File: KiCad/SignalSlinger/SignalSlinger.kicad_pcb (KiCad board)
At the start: 4 copper layers, 94.1 x 59.1 mm, 124 parts, among them J101 Conn_01x02, J102 Conn_01x03, J103 Conn_01x02, J104 Conn_01x02, J105 Conn_01x04, J106 Conn_01x02, J107 DB9 Female, J201 Barrel_Jack_Switch, J203 External Fan Power, J204 Controlled Power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

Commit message: Button Tweak
o Updated on-PCB pushbutton to be the same one used for SignalSnagger
o Updated location of pushbutton to reach only to the edge of the PCB
o Updated Gerbers
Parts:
- SW101: footprint Button_Switch_SMD:SW_SPST_TL3305A -> Button_Switch_SMD:SW_SPST_TL1014BF160QG
- moved SW101 0.31 mm to (82.2, 116.2)
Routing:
- net Net-(C104-Pad1): track 69.8 -> 69.1 mm

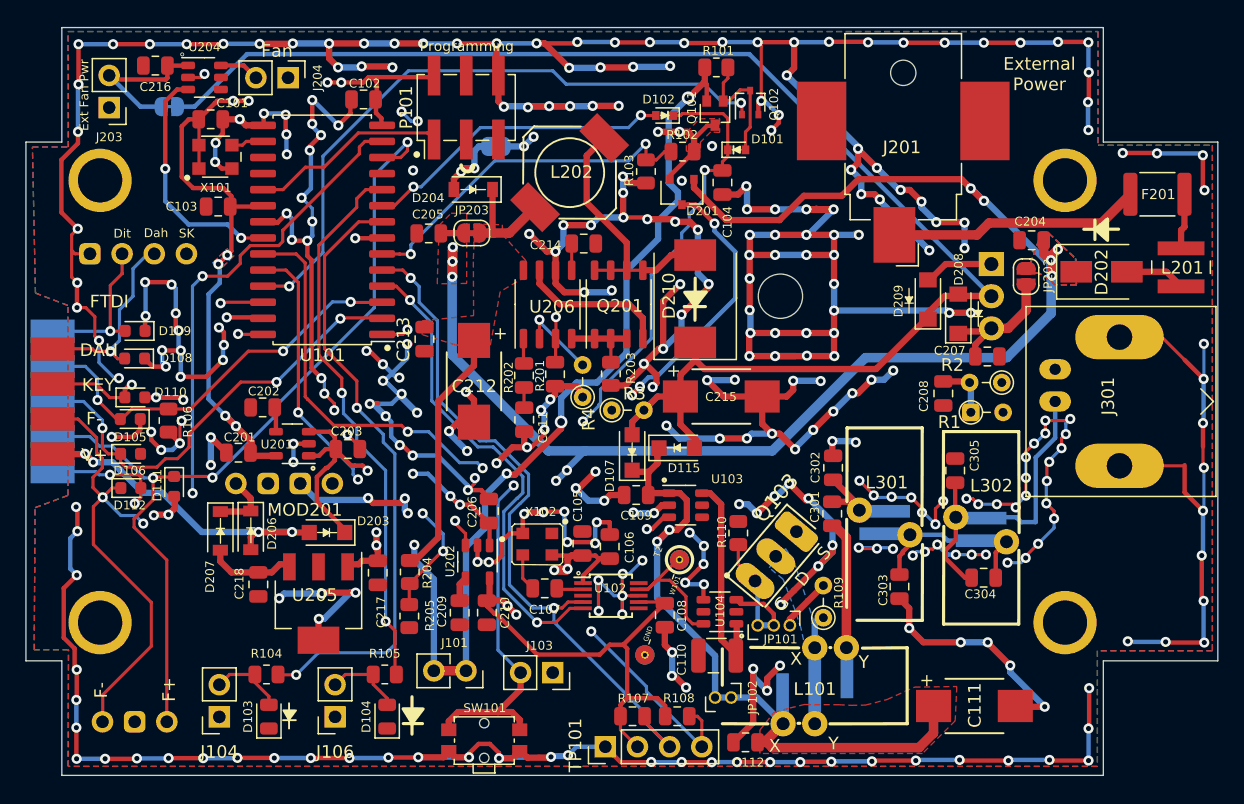
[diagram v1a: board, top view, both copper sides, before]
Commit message: Design Updates
oThe boost regulator was removed from the design.
oAn additional load switch was added to the design.
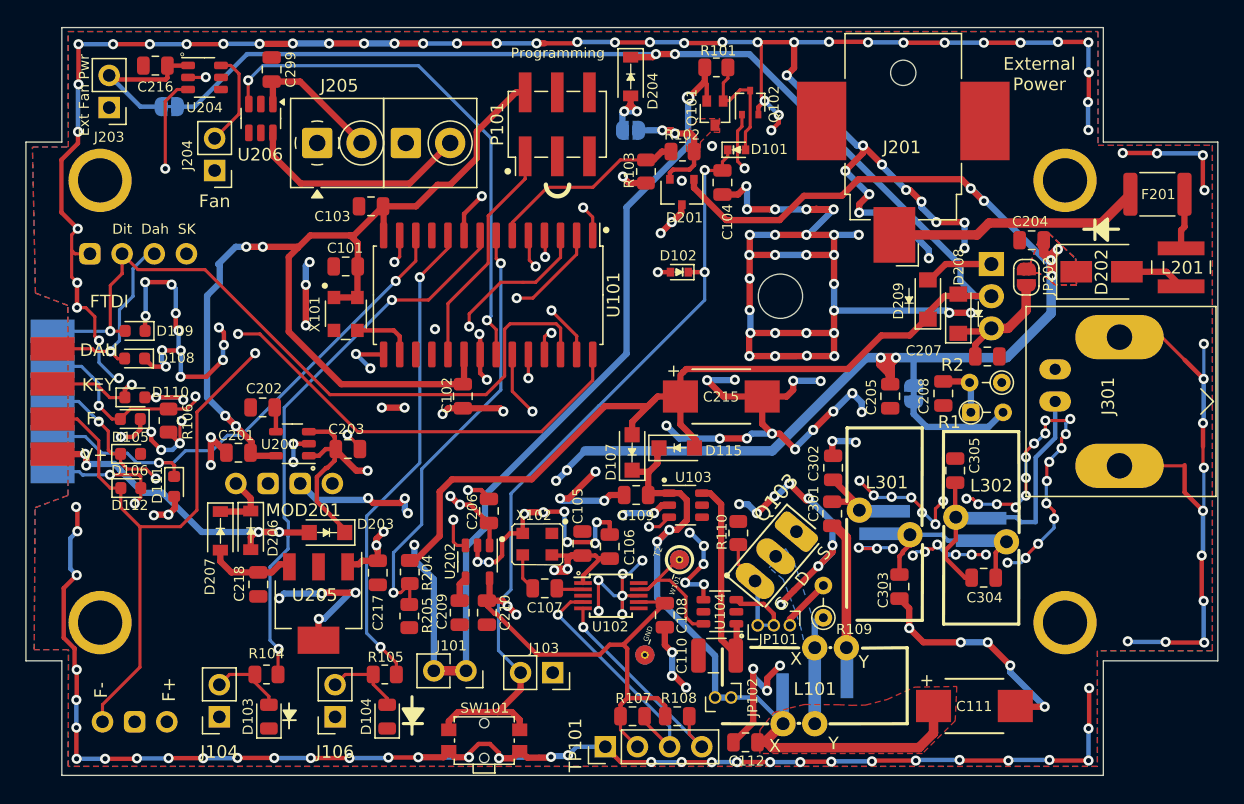
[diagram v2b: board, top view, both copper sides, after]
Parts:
- removed C211: 10nF, Capacitor_SMD:C_0805_2012Metric
- removed C212: 47uF low ESR, Capacitors:C_2917
- removed C213: 10uF, Capacitor_SMD:C_0805_2012Metric
- removed C214: 1uF, Capacitor_SMD:C_0805_2012Metric
- removed D210: B530, Diode_SMD:D_SMC
- removed L202: 6.8uH, Inductors:CDR7D28MN
- removed Q201: RJK0354DSP, Package_SO:SOIC-8_3.9x4.9mm_P1.27mm
- removed R201, R202: 10k, Capacitor_SMD:C_0805_2012Metric
- removed R203: 0.01 0.5W, Resistor_SMD:R_0805_2012Metric
- removed R3, R4: TBD, Resistor_THT:R_Axial_DIN0204_L3.6mm_D1.6mm_P2.54mm_Vertical
- added C299: 10uF, Capacitor_SMD:C_0805_2012Metric, F.Cu at (65.4, 63.2)
- added J205: Controlled Bat Pwr, TerminalBlock_4Ucon:TerminalBlock_4Ucon_1x02_P3.50mm_Horizontal, F.Cu at (69.0, 69.0)
- C111, C215: footprint Capacitors:C_2917 -> Capacitor_Tantalum_SMD:C_2917
- J204: value Controlled Power -> Controlled Fan Power
- JP203: moved to B.Cu
- U206: value MIC2196YM -> TPS22810DBVT; footprint Package_SO:SOIC-8_3.9x4.9mm_P1.27mm -> Package_TO_SOT_SMD:SOT-23-6
- moved C205 38.6 mm to (114.2, 89.0), turned to 90 degrees
- moved JP203 37.1 mm to (116.1, 88.8), turned to -90 degrees
- moved U206 27.0 mm to (64.5, 67.1), turned to -90 degrees
- moved C102 24.7 mm to (80.5, 89.0), turned to -90 degrees
- moved X101 16.1 mm to (71.2, 82.5), turned to 0 degrees
- moved C101 15.8 mm to (71.2, 78.8), turned to 180 degrees
- moved D204 15.3 mm to (93.8, 63.8), turned to -90 degrees
- moved U101 14.1 mm to (82.5, 81.0), turned to -90 degrees
- moved D102 12.4 mm to (97.6, 79.2)
- moved C103 12.1 mm to (73.2, 74.0)
- moved JP204 10.7 mm to (93.8, 68.0)
- moved J204 9.34 mm to (60.9, 71.2), turned to 180 degrees
- moved P101 7.31 mm to (88.0, 67.5)
- moved JP202 0.05 mm to (125.0, 79.6)
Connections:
- net Power_enable renamed Master_Power_enable
- D204 pad 1: Net-(C212-Pad1) -> Vdrive
- JP203 pad 2: Net-(C212-Pad1) -> Vdrive
- R204 pad 2: Net-(C212-Pad1) -> Vdrive
- REF** pad : (no net) -> GND (x4)
- U101 pad 1: BOOST_PWR_ENABLE -> Fan_Contr
- U101 pad 22: Fan_Contr -> Ext_Bat_Contr
- U206 pad 2: Net-(R3-Pad1) -> GND
- U206 pad 3: BOOST_PWR_ENABLE -> Ext_Bat_Contr
- U206 pad 4: Net-(Q201-Pad1) -> unconnected-(U206-CT-Pad4)
- U206 pad 5: Net-(C214-Pad1) -> unconnected-(U206-QOD-Pad5)
- U206 pad 6: GND -> Net-(J205-Pin_4)
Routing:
- net GND: track 895.3 -> 745.0 mm, vias 340 -> 278
- net Ext_Bat_Contr: track 0.00 -> 41.4 mm, vias 0 -> 2
- net Vdrive: track 126.3 -> 162.1 mm, vias 0 -> 2
- net Paddle_Dit: track 25.0 -> 57.9 mm, vias 2 -> 1
- net Straightkey: track 29.3 -> 62.1 mm
- net Net-(C212-Pad1): track 28.0 -> 0.00 mm
- net Fan_Contr: track 18.3 -> 45.8 mm
- net Paddle Dah: track 27.8 -> 55.2 mm
- net FET_DRIVER_ENABLE: track 47.6 -> 21.4 mm, vias 3 -> 2
- net Master_Power_enable: track 51.3 -> 27.3 mm
- net Net-(D210-Pad2): track 20.8 -> 0.00 mm
- net V_ext: track 137.8 -> 118.5 mm, vias 12 -> 11
- net Net-(D106-A1): track 35.3 -> 54.0 mm
- net Net-(D105-A2): track 32.1 -> 50.7 mm
- net +VSW: track 28.3 -> 9.99 mm, vias 4 -> 2
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- removed copper zone on B.Cu, net +3V3
- removed copper zone on F.Cu, net +3V3
- removed copper zone on F.Cu, net Net-(C212-Pad1)
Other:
- board text added: "SignalSlinger 80m Radio-O Fox Transmitter Ver: 3.5; Date: 10-Sep-2025"
- board text removed: "SignalSlinger 80m Radio-O Fox Transmitter Ver: 3.4; Date: 14-Jun-2024"

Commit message: Production Hardware Design Updates
Ver 3.5
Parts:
- added REF**: MountingHole_2mm, MountingHole:MountingHole_2mm, F.Cu at (76.1, 62.5)
- added REF**: MountingHole_2mm, MountingHole:MountingHole_2mm, F.Cu at (72.5, 62.5)
- L302: footprint Inductors:Toroid_T-60_2TH_Vertical -> Inductor_THT:Toroid_T-60_2TH_Vertical2
- moved C305 9.16 mm to (126.2, 101.0), turned to 0 degrees
- moved C303 1.84 mm to (115.1, 102.2)
- moved C304 1.69 mm to (121.3, 101.7), turned to 180 degrees
- moved C111 1.49 mm to (122.3, 113.9)
- moved L101 1.27 mm to (109.6, 111.8)
- turned L302 to 0 degrees
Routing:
- net GND: track 745.0 -> 809.5 mm, vias 278 -> 299
- net Ext_Bat_Contr: track 41.4 -> 33.6 mm
- net Net-(J301-In): track 25.6 -> 18.3 mm
- net Vdrive: track 162.1 -> 168.0 mm
- net Net-(C303-Pad2): track 12.6 -> 8.87 mm
- net Paddle Dah: track 55.2 -> 57.4 mm
- net Master_Power_enable: track 27.3 -> 29.3 mm
- net Frequency Up: track 61.8 -> 63.0 mm
- net Paddle_Dit: track 57.9 -> 58.9 mm
- net Net-(JP102-B): track 23.6 -> 24.3 mm
- net Net-(C301-Pad2): track 5.00 -> 4.36 mm
- net Frequency Down: track 65.2 -> 64.7 mm
- net V3V3_PWR_ENABLE: track 18.5 -> 19.1 mm
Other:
- board text added: "+BAT"
- board text added: "External Battery Control"
- board text added: "Key"
- board text added: "VSW"
- board text removed: "SK"

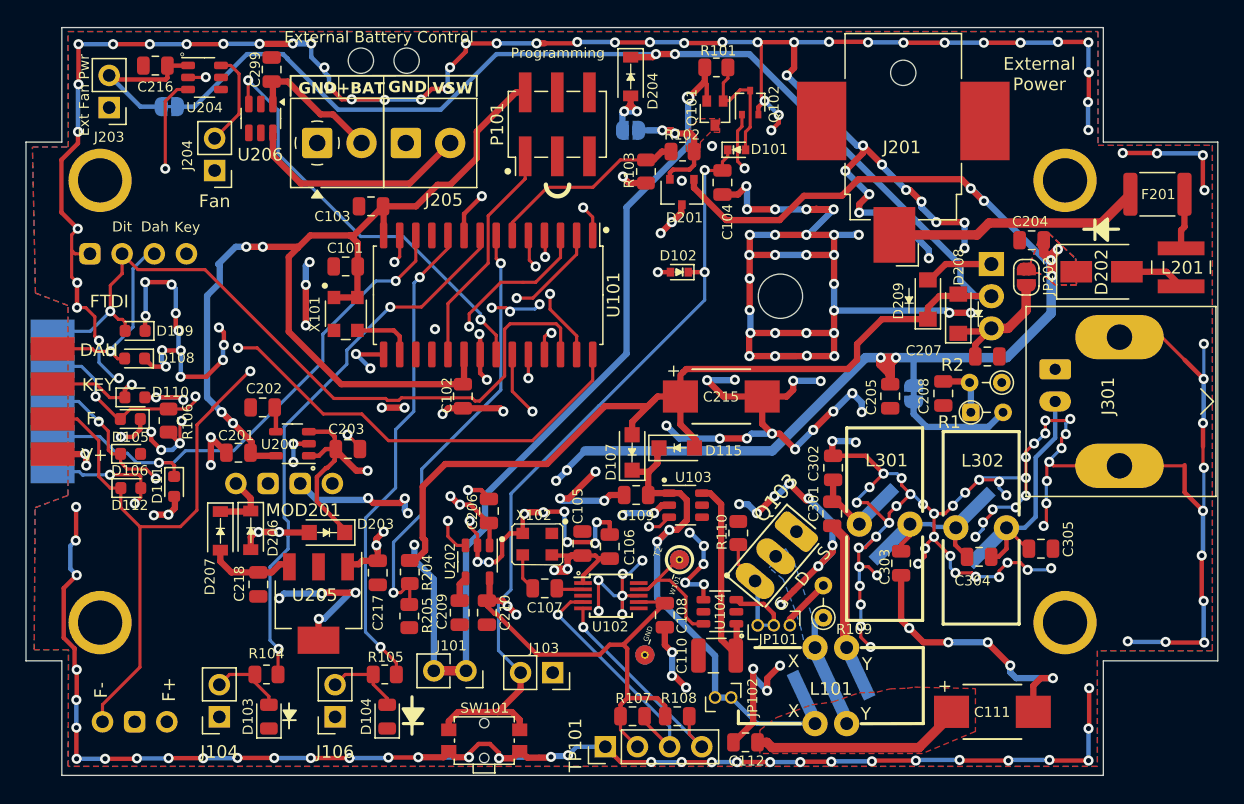
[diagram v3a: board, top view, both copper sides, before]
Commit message: Product File Updates
Increased clearances for better manufacturability.
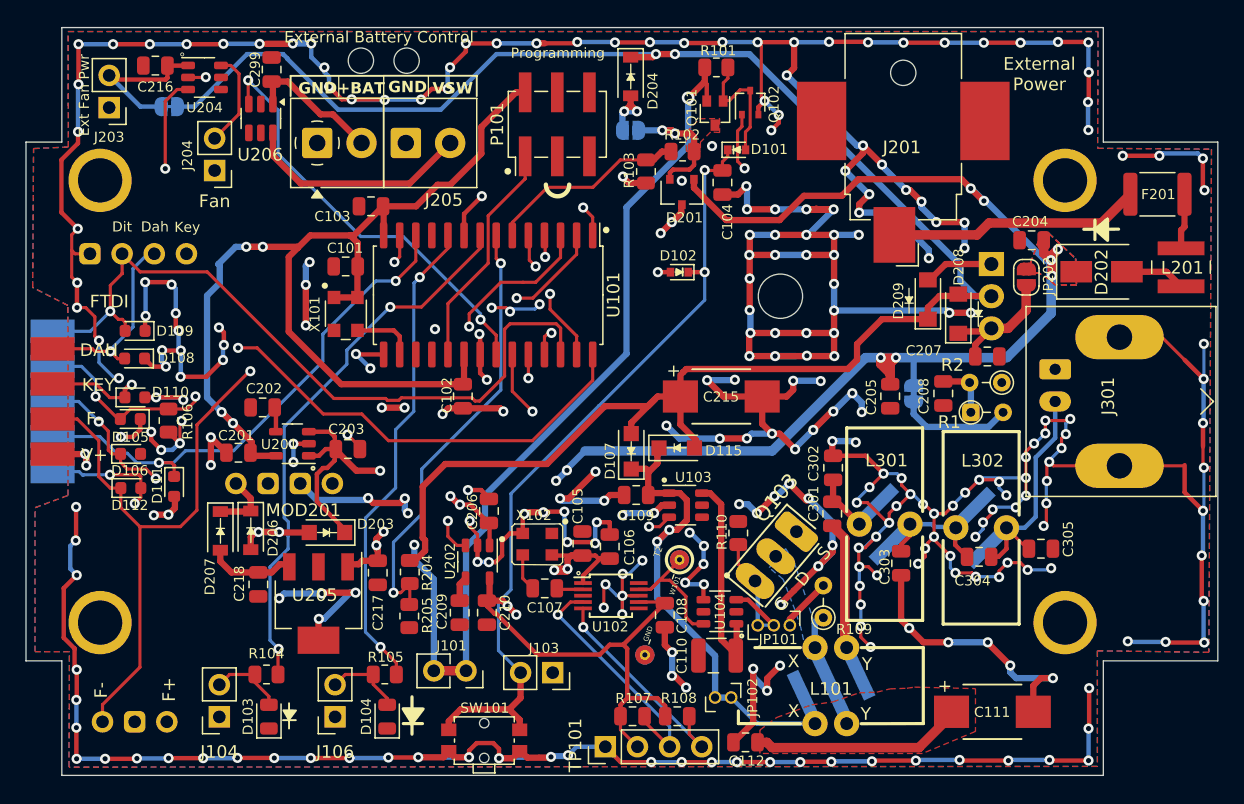
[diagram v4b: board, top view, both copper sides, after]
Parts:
- moved D107 0.11 mm to (93.8, 93.3)
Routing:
- net GND: track 809.5 -> 808.6 mm
- net CLK1: track 11.8 -> 11.0 mm
